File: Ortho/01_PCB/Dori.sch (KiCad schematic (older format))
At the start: 206 parts, among them J1 TYPE-C-31-M12_13, J2 AVR-ISP-6_mod, J3 4PIN, J4 4PIN, J5 TYPE-C-31-M12_13, J6 AVR-ISP-6_mod, K1 KEYSW, K10 KEYSW, K11 KEYSW, K12 KEYSW, K13 KEYSW, K14 KEYSW, K15 KEYSW, K16 KEYSW, K17 KEYSW, K18 KEYSW, K19 KEYSW, K2 KEYSW, K20 KEYSW, K21 KEYSW, K22 KEYSW, K23 KEYSW, K24 KEYSW, K25 KEYSW, K26 KEYSW, K27 KEYSW, K28 KEYSW, K29 KEYSW, K3 KEYSW, K30 KEYSW, K31 KEYSW, K32 KEYSW, K33 KEYSW, K34 KEYSW, K35 KEYSW, K36 KEYSW, K37 KEYSW, K38 KEYSW, K39 KEYSW, K4 KEYSW, K40 KEYSW, K41 KEYSW, K42 KEYSW, K43 KEYSW, K44 KEYSW, K45 KEYSW, K46 KEYSW, K47 KEYSW, K48 KEYSW, K49 KEYSW, K5 KEYSW, K50 KEYSW, K51 KEYSW, K52 KEYSW, K53 KEYSW, K54 KEYSW, K55 KEYSW, K56 KEYSW, K6 KEYSW, K7 KEYSW, K8 KEYSW, K9 KEYSW, SW1 SW_PUSH, SW10 Rotary_Encoder_Switch, SW2 SW_PUSH, SW3 Rotary_Encoder_Switch, SW4 Rotary_Encoder_Switch, SW5 Rotary_Encoder_Switch, SW6 Rotary_Encoder_Switch, SW7 Rotary_Encoder_Switch, SW8 Rotary_Encoder_Switch, SW9 Rotary_Encoder_Switch, U1 ATMEGA32U4, U10 HOLE, U11 HOLE, U12 ATMEGA32U4, U13 HOLE, U14 HOLE, U15 HOLE, U16 HOLE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

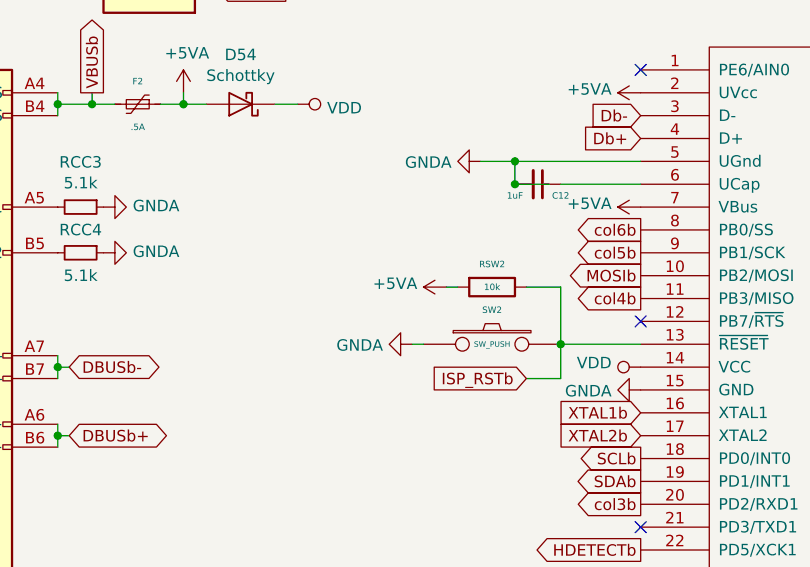
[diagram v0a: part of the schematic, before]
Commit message: Moved USB port
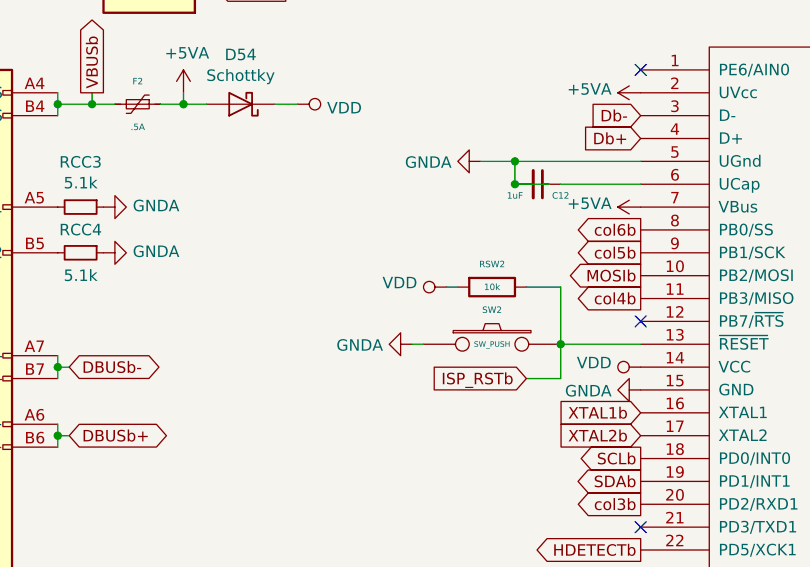
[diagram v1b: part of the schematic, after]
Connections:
- net +5VA: no longer RSW2.2
- net VDD: now also RSW2.2
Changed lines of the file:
@@
-$EndComp
-$Comp
-L power:+5VA #PWR0149
-U 1 1 5FD8BF6F
-P 16600 8100
-F 0 "#PWR0149" H 16600 7950 50  0001 C CNN
-F 1 "+5VA" V 16615 8227 50  0000 L CNN
-F 2 "" H 16600 8100 50  0001 C CNN
-F 3 "" H 16600 8100 50  0001 C CNN
-	1    16600 8100
-	0    -1   -1   0
 $EndComp
 $Comp
@@
 	1    0    0    -1
 $EndComp
+Wire Notes Line
+	19150 11550 19150 10100
+Wire Notes Line
+	17500 11550 19150 11550
+Wire Notes Line
+	17500 10100 19150 10100
 $Comp
 L power:+5VA #PWR0158
@@
 	0    1    1    0
 $EndComp
-Wire Notes Line
-	19150 11550 19150 10100
-Wire Notes Line
-	17500 11550 19150 11550
-Wire Notes Line
-	17500 10100 19150 10100
+$Comp
+L power:VDD #PWR0149
+U 1 1 5F33E2FA
+P 16600 8100
+F 0 "#PWR0149" H 16600 7950 50  0001 C CNN
+F 1 "VDD" V 16618 8227 50  0000 L CNN
+F 2 "" H 16600 8100 50  0001 C CNN
+F 3 "" H 16600 8100 50  0001 C CNN
+	1    16600 8100
+	0    -1   -1   0
+$EndComp
 $EndSCHEMATC
